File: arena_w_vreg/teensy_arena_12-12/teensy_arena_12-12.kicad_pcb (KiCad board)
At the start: 4 copper layers, 254 x 254 mm, 87 parts, among them J1 Barrel_Jack, J2 Conn_01x04, J3 Conn_01x04, P1 CONN15, P10 CONN15, P11 CONN15, P12 CONN15, P2 CONN15, P3 CONN15, P4 CONN15, P5 CONN15, P6 CONN15, P7 CONN15, P8 CONN15, P9 CONN15, Q2 MOSFET_NCHAN, SW1 SW_SPDT, U1 TXB0108PW, U10 AZ1084-5.0, U11 AZ1084-5.0, U12 AZ1084-5.0, U13 AZ1084-5.0, U14 AZ1084-5.0, U15 AZ1084-5.0, U16 AZ1084-5.0, U17 AZ1084-5.0, U18 Teensy4.1, U2 TXB0108PW, U3 TXB0108PW, U4 TXB0108PW, U5 TXB0108PW, U6 AZ1084-5.0, U7 AZ1084-5.0, U8 AZ1084-5.0, U9 AZ1084-5.0

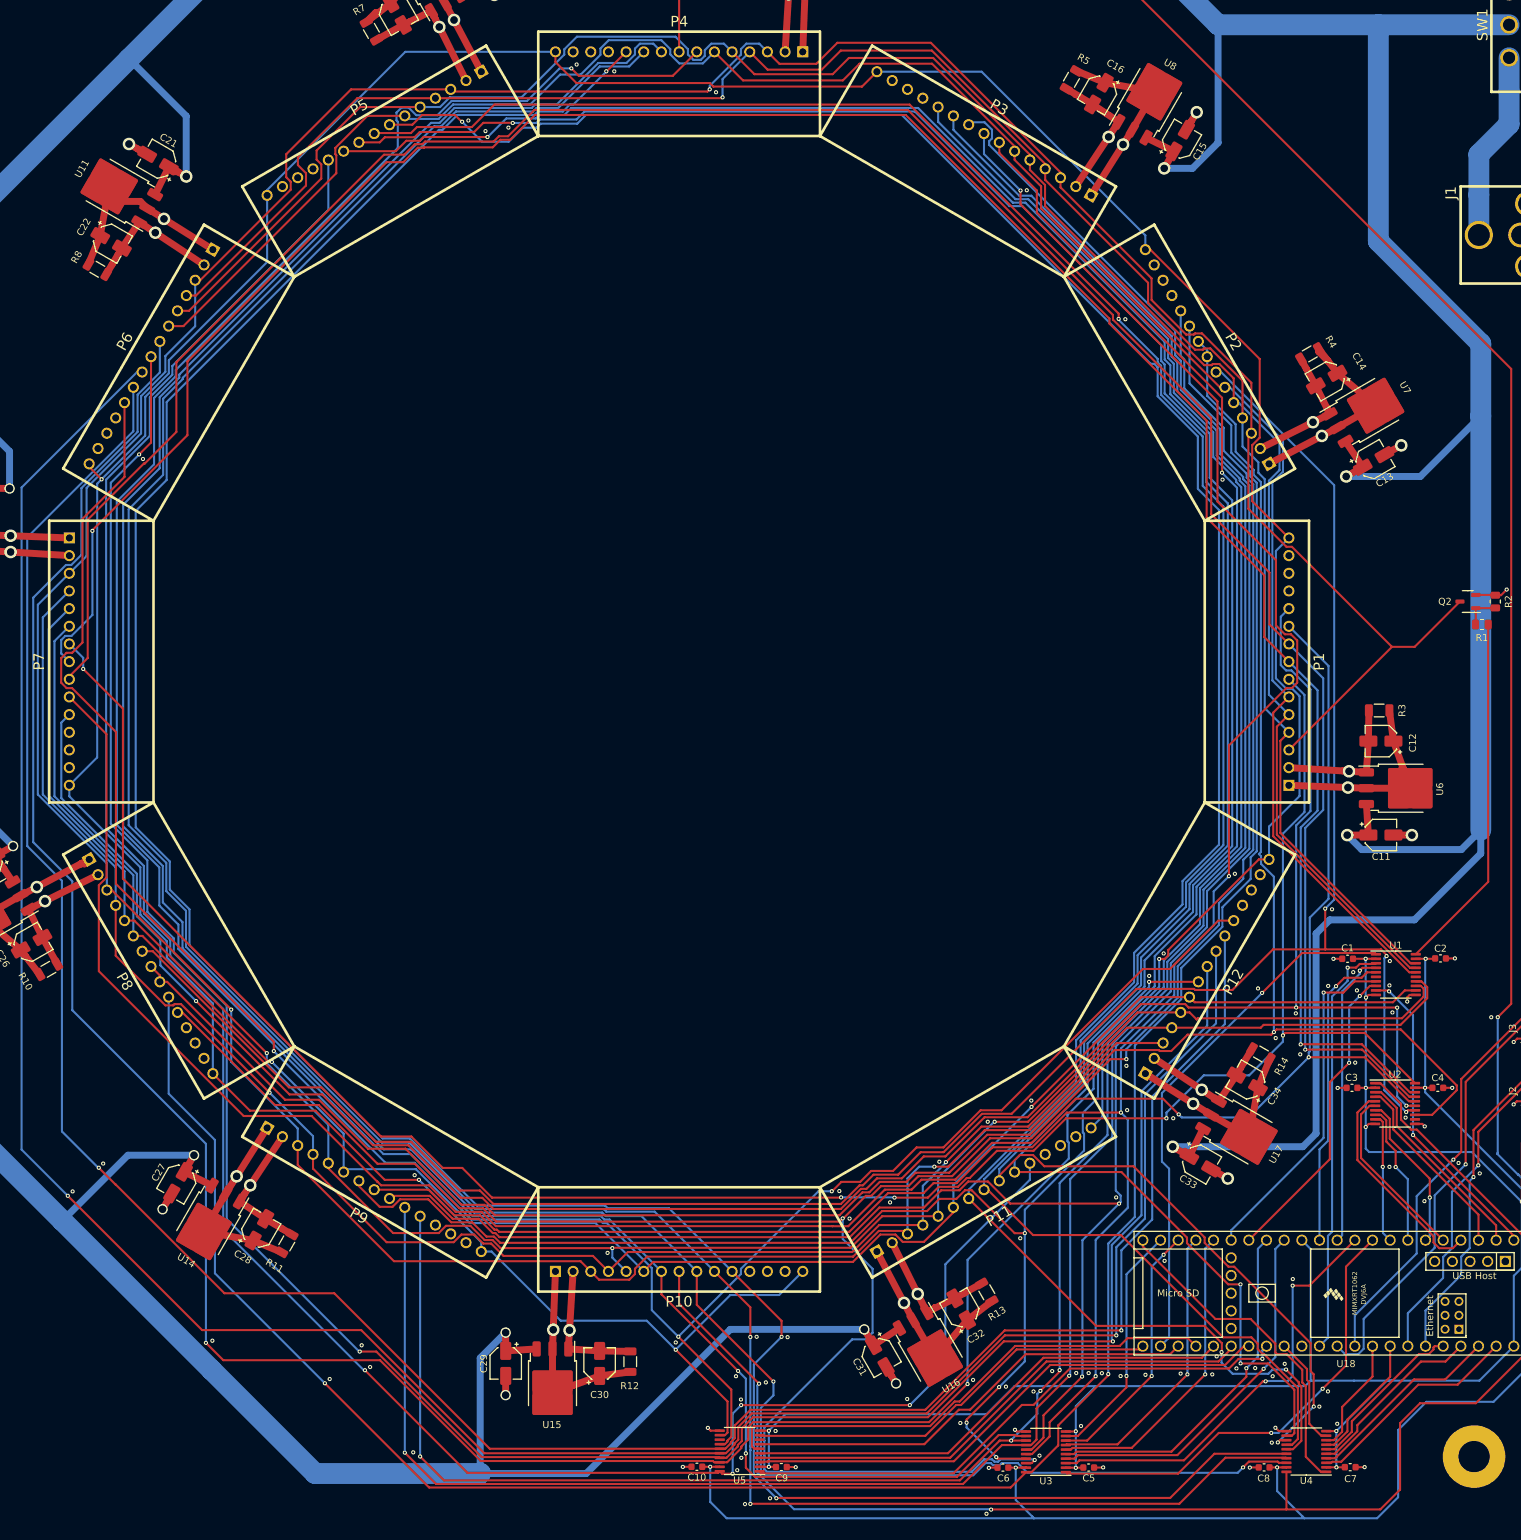
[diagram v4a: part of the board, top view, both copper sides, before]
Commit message: Worked on routing 12-12 teensy arena/controller with vreg.
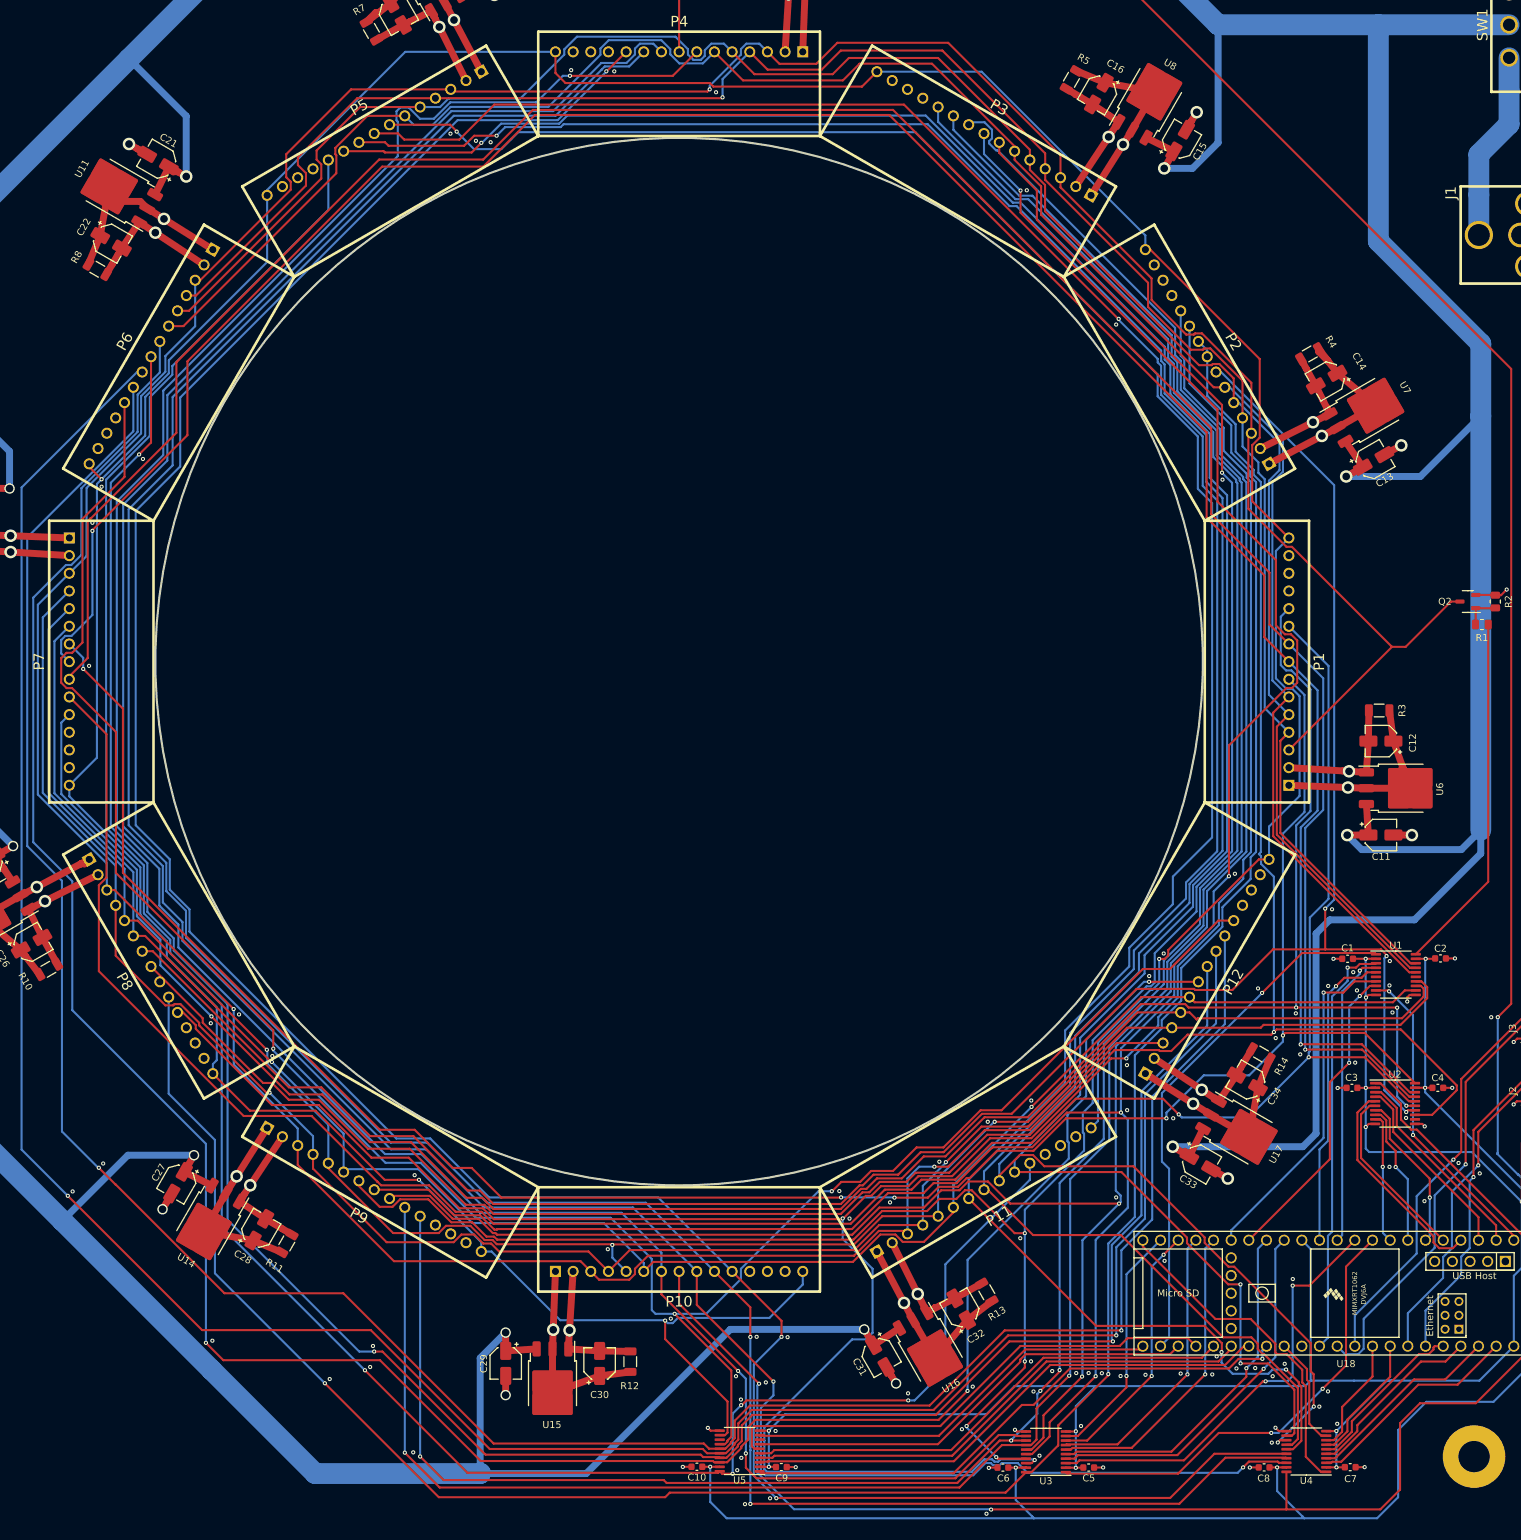
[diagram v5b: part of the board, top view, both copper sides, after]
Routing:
- net /Level Shifters/PAN5V.EXT_INT: track 576.0 -> 580.3 mm
- net /Level Shifters/PAN5V.CS_20: track 339.1 -> 335.4 mm
- net /Level Shifters/PAN5V.CS_22: track 345.3 -> 343.1 mm
- net /Level Shifters/PAN5V.CS_29: track 314.1 -> 316.1 mm
- net /Level Shifters/PAN5V.CS_19: track 382.1 -> 380.2 mm
- net /Level Shifters/PAN5V.CS_23: track 338.7 -> 337.0 mm
- net /Panel Headers/RESET: track 580.7 -> 582.4 mm
- net /Level Shifters/PAN5V.CS_18: track 384.9 -> 383.4 mm
- net /Level Shifters/PAN5V.CS_01: track 348.1 -> 346.7 mm
- net /Level Shifters/PAN5V.CS_17: track 384.7 -> 383.3 mm
- net /Level Shifters/PAN5V.CS_15: track 354.6 -> 355.9 mm
- net /Level Shifters/PAN5V.CS_02: track 351.7 -> 350.4 mm
- net /Level Shifters/PAN5V.SCK_0: track 292.5 -> 293.7 mm
- net /Level Shifters/PAN5V.MISO_0: track 299.2 -> 300.4 mm
- net /Level Shifters/PAN5V.CS_08: track 355.7 -> 356.8 mm
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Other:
- outline, holes or cut-outs redrawn

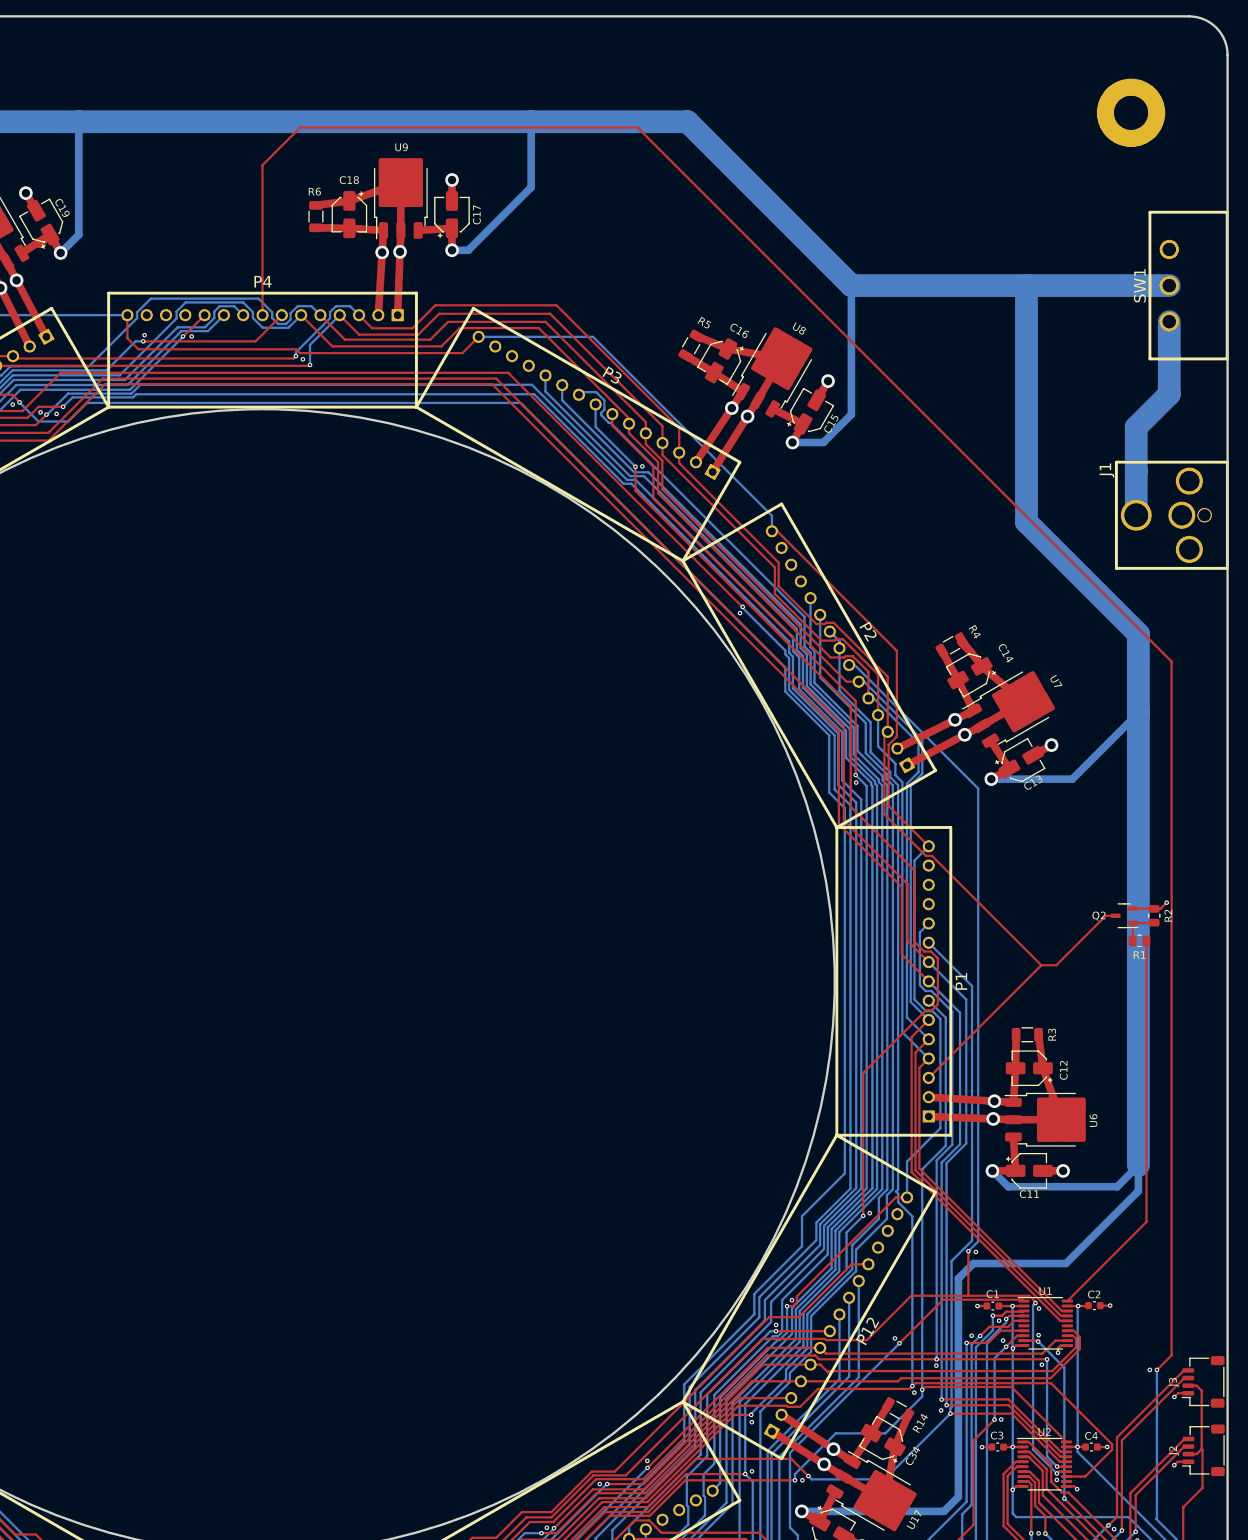
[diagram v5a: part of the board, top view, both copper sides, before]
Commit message: Added annotations to silkscreen.
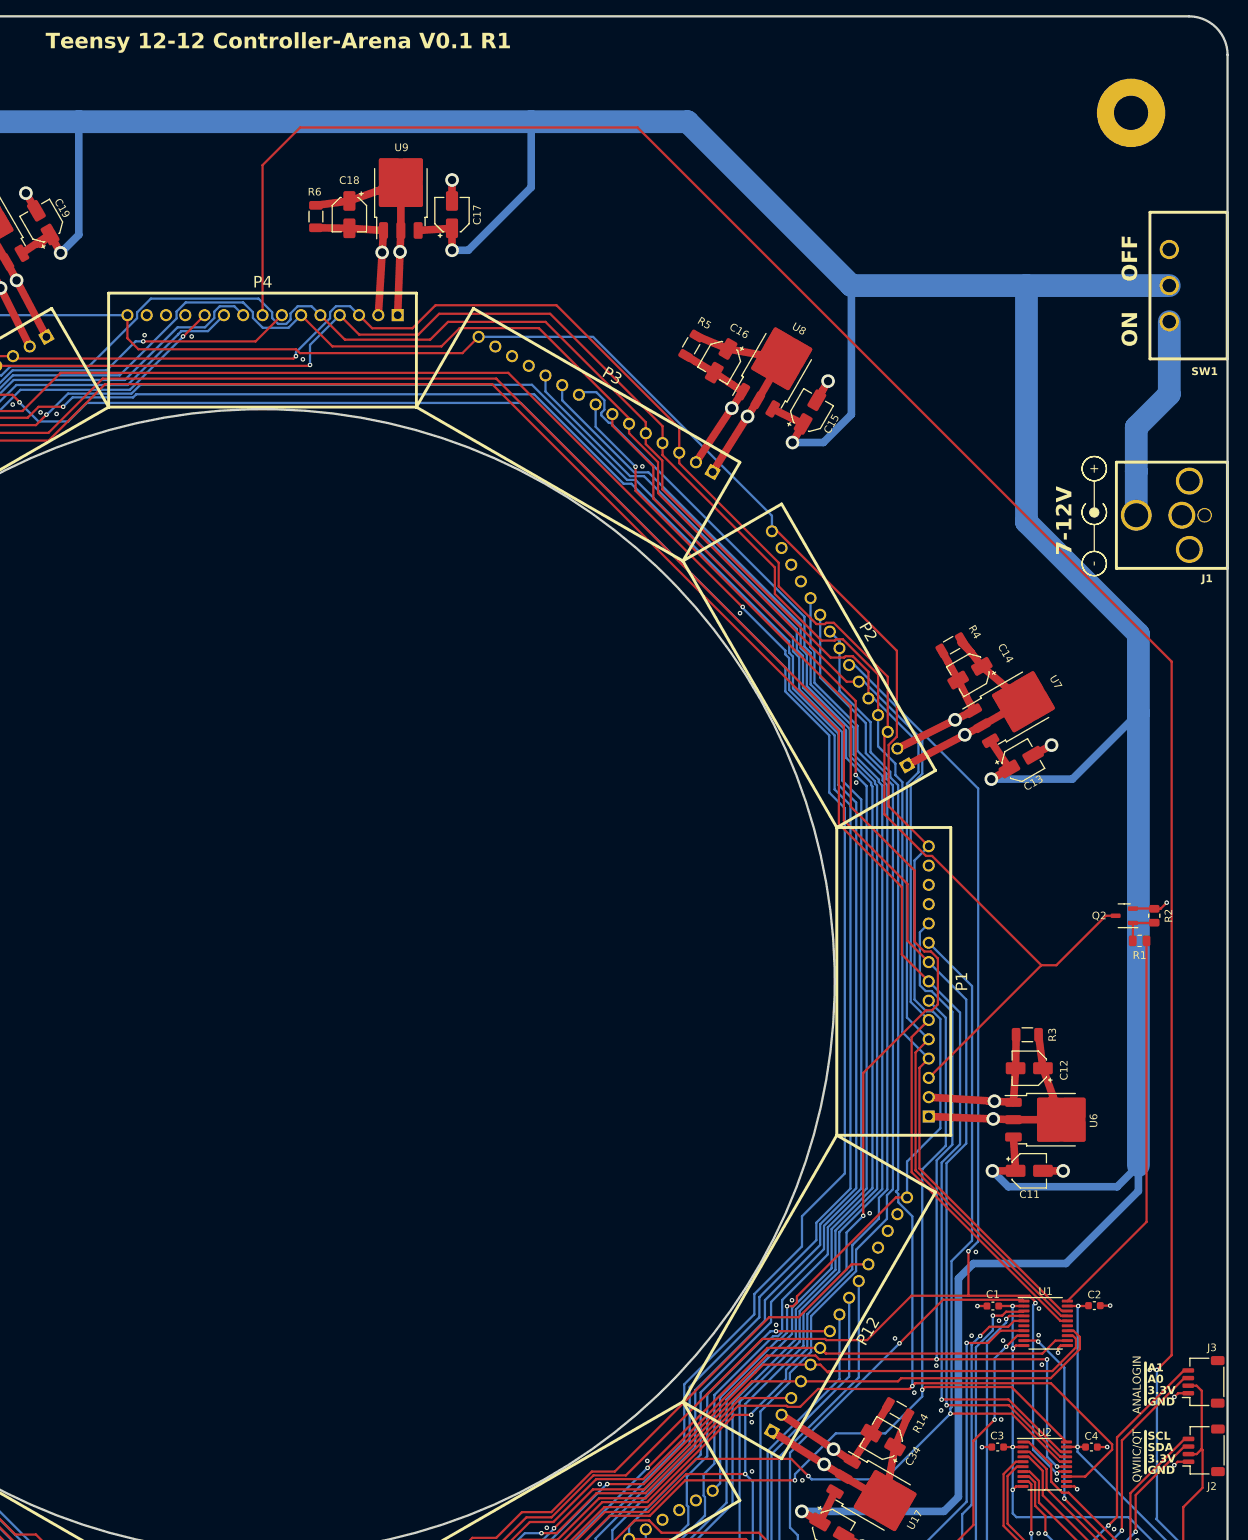
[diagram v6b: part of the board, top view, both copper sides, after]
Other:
- board text added: "3.3V"
- board text added: "7-12V"
- board text added: "A0"
- board text added: "A1"
- board text added: "ANALOGIN"
- board text added: "GND"
- board text added: "ON OFF"
- board text added: "QWIIC/QT"
- board text added: "SCL"
- board text added: "SDA"
- board text added: "Teensy 12-12 Controller-Arena V0.1 R1"
